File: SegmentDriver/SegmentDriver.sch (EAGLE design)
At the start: 220 parts, among them IC1 PCA9555PW, IC2 ATMEGA644A, IC3 4511D, K1 691313710002, K17 61200621621, K18 61201021621, K2 691322310002, K4 691313710002, K5 691322310002, Q1 MOSFET-NCHANNEL-FDMS5672, Q10 DMP2215L-7, Q11 DMP2215L-7, Q2 MOSFET-NCHANNEL-FDMS5672, Q3 MOSFET-NCHANNEL-FDMS5672, Q4 MOSFET-NCHANNEL-FDMS5672, Q5 MOSFET-NCHANNEL-FDMS5672, Q6 MOSFET-NCHANNEL-FDMS5672, Q7 MOSFET-NCHANNEL-FDMS5672, Q8 MOSFET-NCHANNEL-FDMS5672, Q9 MOSFET-NCHANNEL-FDMS5672, U1 FOD8321, U10 FOD8321, U13 DS1307SO8-TIGHT, U2 FOD8321, U3 FOD8321, U5 FOD8321, U6 FOD8321, U7 FOD8321, U8 FOD8321, U9 FOD8321, X1 32.768kHz

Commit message: routing rtd inputs
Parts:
- removed H9: MOUNT-PAD-ROUND2,0, simbits:MOUNT-PAD-ROUND2,0
- removed KB1: 53261-03, con-molex:53261-03
- removed KT1, KT2: 691210910004, Wurth_Elektronik_Electromechanic_Terminal_Blocks_Connectors_rev15d:691210910004
- removed LED8: AMBER, adafruit:LEDCHIPLED_0603
- removed Q10: DMP2215L-7, simbits:DMP2215L-7
- removed R69: 33R, simbits:EXBV8V330JV
- added $2_206_$_2016-11-07_20-18-07: MOUNT-HOLE2.0, simbits:MOUNT-HOLE2.0
- added K6: 61200621621, Wire-to-Board:61200621621
- added K7: 61201021621, Wire-to-Board:61201021621
- added LED4: (no value), adafruit:LEDCHIPLED_0603
- added R61: 1k, simbits:EXBV8V330JV
- added U17: (no value), LINE_DRIVERS:ISL83078E
- added Y2: 32.768kHz, SparkFun-FreqCtrl:CRYSTALEPSONMC146
- C1: value 0.1uF -> 470UF; device rcl:C-EUC1206K -> Panasonic-EEEFK_EEEFP:EEE-FK1J471AM-CASE-J16; OC_FARNELL (none) -> 2284670
- C11: value 220UF -> 12pF; device Panasonic-EEEFK_EEEFP:EEE-FK1J221AQ-CASE-H13 -> rcl:C-EUC0603K
- C12: value 0.1uF -> 12pF; device rcl:C-EUC1206K -> rcl:C-EUC0603K
- C13, C6: value 220UF -> 0.1uF; device Panasonic-EEEFK_EEEFP:EEE-FK1J221AQ-CASE-H13 -> rcl:C-EUC0603K
- C14, C5, C7, C8, C9: device rcl:C-EUC1206K -> rcl:C-EUC0603K
- C15, C17, C18: value 220UF -> 0.1uF; device Panasonic-EEEFK_EEEFP:EEE-FK1J221AQ-CASE-H13 -> rcl:C-EUC1206K
- C19, C20, C21, C22, C23: device rcl:C-EUC0603K -> rcl:C-EUC1206K
- C2: value 0.1uF -> 220UF; device rcl:C-EUC1206K -> Panasonic-EEEFK_EEEFP:EEE-FP1V221AP-CASE-F
- C24, C26, C27, C28, C29, C30: value 0.1uF -> 220UF; device rcl:C-EUC0603K -> Panasonic-EEEFK_EEEFP:EEE-FK1J221AQ-CASE-H13
- C3: value 220UF -> 470UF; device Panasonic-EEEFK_EEEFP:EEE-FK1J221AQ-CASE-H13 -> Panasonic-EEEFK_EEEFP:EEE-FK1J471AM-CASE-J16
- C31, C32: value 12pF -> 220UF; device rcl:C-EUC0603K -> Panasonic-EEEFK_EEEFP:EEE-FK1J221AQ-CASE-H13
- C34, C37, C60: value 1uF -> 0.1uF
- C39, C40, C41: value 0.1uF -> 1uF
- C4: device Panasonic-EEEFK_EEEFP:EEE-FK1J221AQ-CASE-H13 -> Panasonic-EEEFK_EEEFP:EEE-FP1V221AP-CASE-F
- C72, C76: value 470UF -> 0.1uF; device Panasonic-EEEFK_EEEFP:EEE-FK1J471AM-CASE-J16 -> rcl:C-EUC0603K
- C74, C75: value 220UF -> 0.1uF; device Panasonic-EEEFK_EEEFP:EEE-FP1V221AP-CASE-F -> rcl:C-EUC0603K
- H5: value MOUNT-HOLE2.0 -> MOUNT-PAD-ROUND2,0; device simbits:MOUNT-HOLE2.0 -> simbits:MOUNT-PAD-ROUND2,0
- IC1: value PCA9555PW -> ATMEGA644A; device micro-philips:PCA9555PW -> atmel:ATMEGA644A
- IC2: value ATMEGA644A -> PCA9555PW; device atmel:ATMEGA644A -> micro-philips:PCA9555PW
- K17: value 61200621621 -> 691210910004; device Wire-to-Board:61200621621 -> Wurth_Elektronik_Electromechanic_Terminal_Blocks_Connectors_rev15d:691210910004
- K18: value 61201021621 -> 691210910004; device Wire-to-Board:61201021621 -> Wurth_Elektronik_Electromechanic_Terminal_Blocks_Connectors_rev15d:691210910004
- K2: value 691322310002 -> 691313710002; device Wurth_Elektronik_Electromechanic_Terminal_Blocks_Connectors_rev15d:691322310002 -> Wurth_Elektronik_Electromechanic_Terminal_Blocks_Connectors_rev15d:691313710002
- K3: value (none) -> 691322310002; device Wurth_Elektronik_Electromechanic_Input-Output_Connectors_rev15c:615016149521 -> Wurth_Elektronik_Electromechanic_Terminal_Blocks_Connectors_rev15d:691322310002
- K4: value 691313710002 -> 691322310002; device Wurth_Elektronik_Electromechanic_Terminal_Blocks_Connectors_rev15d:691313710002 -> Wurth_Elektronik_Electromechanic_Terminal_Blocks_Connectors_rev15d:691322310002
- K5: value 691322310002 -> (none); device Wurth_Elektronik_Electromechanic_Terminal_Blocks_Connectors_rev15d:691322310002 -> Wurth_Elektronik_Electromechanic_Input-Output_Connectors_rev15c:615016149521
- LED1: value 7-SEG_SA02-107 -> (none); device display-kingbright-2:7-SEG_SA02-107 -> adafruit:LEDCHIPLED_0603
- LED5, LED6: value (none) -> AMBER
- LED7: value AMBER -> 7-SEG_SA02-107; device adafruit:LEDCHIPLED_0603 -> display-kingbright-2:7-SEG_SA02-107
- R1: value 330 -> 2K4
- R10: value 10k -> 330
- R11, R12: value 100k -> 330
- R13, R14, R15, R16, R17: value 0R -> 330
- R18: value 1k -> 330
- R19, R20, R21, R29, R30, R34, R36: value 0R -> 100k
- R2: value 330 -> 1.2K
- R22, R23, R24, R25, R26, R27: value 0R -> 33R; device rcl:R-EU_R0603 -> simbits:EXBV8V330JV; MPN (none) -> EXBV8V470JV
- R28: value 10k -> 100k
- R3, R9: value 330 -> 10k
- R31, R35: value 1k -> 100k
- R32, R33: value 4.7k -> 100k
- R37, R38, R39, R40, R41, R42, R43, R44, R45, R46: value 100k -> 0R
- R4, R7, R8: value 330 -> 1k
- R47: value 1.2K -> 0R
- R48: value 2K4 -> 0R
- R49, R50, R51, R52: value 33R -> 0R; device simbits:EXBV8V330JV -> rcl:R-EU_R0603; MPN EXBV8V470JV -> (none)
- R5, R6: value 330 -> 4.7k
- R53, R54: value 1k -> 0R
- R55: value 33R -> 1k; device simbits:EXBV8V330JV -> rcl:R-EU_R0603; MPN EXBV8V470JV -> (none)
- R56: value 47R -> 1k; device simbits:EXBV8V330JV -> rcl:R-EU_R0603; MPN EXBV8V470JV -> (none)
- R57: value 47R -> 10k; device simbits:EXBV8V330JV -> rcl:R-EU_R0603; MPN EXBV8V470JV -> (none)
- R58: value 10k -> 47R; device rcl:R-EU_R0603 -> simbits:EXBV8V330JV; MPN (none) -> EXBV8V470JV
- R59: MPN EXBV8V102JV -> EXBV8V470JV
- R60: value 1k -> 47R
- U1: value FOD8321 -> DS1307SO8-TIGHT; device simbits:FOD8321 -> SparkFun-FreqCtrl:DS1307SO8-TIGHT
- U11: value (none) -> FOD8321; device simbits:ADS1X48IPW -> simbits:FOD8321
- U13: value DS1307SO8-TIGHT -> (none); device SparkFun-FreqCtrl:DS1307SO8-TIGHT -> simbits:ADS1X48IPW
- U15: value (none) -> DMP2215L-7; device LINE_DRIVERS:ISL83078E -> simbits:DMP2215L-7
- U2: value FOD8321 -> (none); device simbits:FOD8321 -> adafruit:PCA9685
- U4: value (none) -> FOD8321; device adafruit:PCA9685 -> simbits:FOD8321
- X1: value 32.768kHz -> 53261-03; device SparkFun-FreqCtrl:CRYSTALEPSONMC146 -> con-molex:53261-03
- renumbered KB2 to X2, KB3 to X3, KB4 to X4, KB5 to X5, KB6 to X6, KD1 to K15, KD2 to K16, KS1 to K8, KS2 to K9, KS3 to K10, KS4 to K11, KS5 to K12, KS6 to K13, KS7 to K14, KT3 to K19, KT4 to K20, KT5 to K21, KT6 to K22, KT7 to K23, KTD1 to K24, KTD2 to K25, Q11 to U16, RESET_SW to SW1
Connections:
- removed net N$77: R52.5, U12.SCLK@28
- removed net N$78: R52.6, U12.DOUT/!DRDY!@26
- removed net N$79: R52.7, U12.DIN@27
- removed net N$80: R52.8, U12.!CS!@24
- removed net N$81: R55.5, U12.!DRDY!@25
- removed net N$82: R55.8, U12.START@23
- new net AD1_REFN0: C43.2, C44.1, R29.2, U12.REFN0/GPIO1@6
- new net AD1_REFP0: C42.2, C43.1, R28.2, U12.REFP0/GPIO0@5
- new net AD2_REFN0: C46.2, C47.1, R31.2, U13.REFN0/GPIO1@6
- new net AD2_REFP0: C45.2, C46.1, R30.2, U13.REFP0/GPIO0@5
- new net AD3_REFN0: C49.2, C50.1, R33.2, U14.REFN0/GPIO1@6
- new net AD3_REFP0: C48.2, C49.1, R32.2, U14.REFP0/GPIO0@5
- net !RESET: now also IC1.RESET, K6.5, K7.6, R3.1; no longer IC2.RESET, K17.5, K18.6, R28.1
- net +12V: now also C15.1, C17.1, C18.1, C19.1, C20.1, C21.1, C22.1, C23.1, C4.1, C6.2, K3.1, K4.2, R2.2, U11.VDD@6, U4.VDD@6; no longer C1.1, C12.1, C14.1, C5.1, C7.1, C74.1, C75.1, C77.2, C8.1, C9.1, K2.1, K5.2, R47.2, U1.VDD@6, U2.VDD@6
- net +24V: now also C1.1, C3.1, C5.2, K2.2, R1.2; no longer C72.1, C76.1, C78.2, K4.2, R48.2
- net +5V: now also C14.1, C78.1, IC2.VDD, R57.2, R9.2, U15.S, U17.VCC, U2.VDD, X1-1.S; no longer C10.1, C73.1, IC1.VDD, KB1-1.S, Q10.S, R10.2, R58.2, U15.VCC, U4.VDD
- net 5V: now also C10.2, C7.2, C8.2, C9.2, IC1.AVCC, IC1.VCC, IC1.VCC@1, IC1.VCC@2, K6.2, K7.4, R3.2, R5.2, R6.2, U1.VCC; no longer C26.2, C27.2, C28.2, C30.2, IC2.AVCC, IC2.VCC, IC2.VCC@1, IC2.VCC@2, K17.2, K18.4, R28.2, R32.2, R33.2, U13.VCC
- net AD1_!CS: now also R22.2; no longer R69.1
- net AD1_!DRDY: now also R22.3; no longer R49.4
- net AD1_!RESET: now also R19.1, U12.!RESET!@4; no longer R11.1, U11.!RESET!@4
- net AD1_AIN0: now also K17.4, U12.AIN0/IEXC@11; no longer KT1.4, U11.AIN0/IEXC@11
- net AD1_AIN1: now also C51.2, C54.1, R37.1, U12.AIN1/IEXC@12; no longer C19.2, C20.1, R13.1, U11.AIN1/IEXC@12
- net AD1_AIN2: now also C51.1, C57.2, R38.1, U12.AIN2/IEXC/GPIO2@17; no longer C19.1, C22.2, R14.1, U11.AIN2/IEXC/GPIO2@17
- net AD1_AIN3: now also K18.4, U12.AIN3/IEXC/GPIO3@18; no longer KT2.4, U11.AIN3/IEXC/GPIO3@18
- net AD1_AIN4: now also C52.2, C55.1, R39.1, U12.AIN4/IEXC/GPIO4@13; no longer C23.2, C24.1, R15.1, U11.AIN4/IEXC/GPIO4@13
- net AD1_AIN5: now also C52.1, C58.2, R40.1, U12.AIN5/IEXC/GPIO5@14; no longer C23.1, C38.2, R16.1, U11.AIN5/IEXC/GPIO5@14
- net AD1_AIN6: now also C53.2, C56.1, R41.1, U12.AIN6/IEXC/GPIO6@15; no longer C39.2, C40.1, R17.1, U11.AIN6/IEXC/GPIO6@15
- net AD1_AIN7: now also C53.1, C59.2, R42.1, U12.AIN7/IEXC/GPIO7@16; no longer C39.1, C41.2, R19.1, U11.AIN7/IEXC/GPIO7@16
- net AD1_BIASP: now also K17.1, K18.1, R28.1, R34.2; no longer KT1.1, KT2.1, R38.2, R39.1
- net AD1_IEXC1: now also U12.IEXC1@20
- net AD1_START: now also R22.1; no longer R49.1
- net AD2_!CS: now also R24.2; no longer R52.1
- net AD2_!DRDY: now also R24.3; no longer R55.4
- net AD2_!RESET: now also R20.1, U13.!RESET!@4; no longer R12.1, U12.!RESET!@4
- net AD2_AIN0: now also U13.AIN0/IEXC@11; no longer U12.AIN0/IEXC@11
- net AD2_AIN1: now also C60.2, C63.1, R43.1, U13.AIN1/IEXC@12; no longer C42.2, C43.1, R20.1, U12.AIN1/IEXC@12
- net AD2_AIN2: now also C60.1, C66.2, R44.1, U13.AIN2/IEXC/GPIO2@17; no longer C42.1, C44.2, R21.1, U12.AIN2/IEXC/GPIO2@17
- net AD2_AIN3: now also U13.AIN3/IEXC/GPIO3@18; no longer U12.AIN3/IEXC/GPIO3@18
- net AD2_AIN4: now also C61.2, C64.1, R45.1, U13.AIN4/IEXC/GPIO4@13; no longer C45.2, C46.1, R22.1, U12.AIN4/IEXC/GPIO4@13
- net AD2_AIN5: now also C61.1, C67.2, R46.1, U13.AIN5/IEXC/GPIO5@14; no longer C45.1, C47.2, R23.1, U12.AIN5/IEXC/GPIO5@14
- net AD2_AIN6: now also C62.2, C65.1, R47.1, U13.AIN6/IEXC/GPIO6@15; no longer C48.2, C49.1, R24.1, U12.AIN6/IEXC/GPIO6@15
- net AD2_AIN7: now also C62.1, C68.2, R48.1, U13.AIN7/IEXC/GPIO7@16; no longer C48.1, C50.2, R25.1, U12.AIN7/IEXC/GPIO7@16
- net AD2_BIASP: now also R30.1, R32.1, R35.2, R36.2; no longer R41.2, R42.1, R44.2, R45.1
- net AD2_IEXC1: now also U13.IEXC1@20
- net AD2_START: now also R24.1; no longer R55.1
- net AD3_!CS: now also R26.2; no longer R51.1
- net AD3_!DRDY: now also R26.3; no longer R50.4
- net AD3_!RESET: now also R21.1; no longer R37.1
- net AD3_AIN1: now also C69.2, C72.1, R49.1; no longer C51.2, C52.1, R26.1
- net AD3_AIN2: now also C69.1, C75.2, R50.1; no longer C51.1, C53.2, R27.1
- net AD3_AIN4: now also C70.2, C73.1, R51.1; no longer C54.2, C55.1, R29.1
- net AD3_AIN5: now also C70.1, C76.2, R52.1; no longer C54.1, C56.2, R30.1
- net AD3_AIN6: now also C71.2, C74.1, R53.1; no longer C57.2, C58.1, R34.1
- net AD3_AIN7: now also C71.1, C77.2, R54.1; no longer C57.1, C59.2, R36.1
- net AD3_IEXC1: now also U14.IEXC1@20
- net AD3_START: now also R26.1; no longer R50.1
- net AGND: now also C24.2, C26.2, C27.2, C28.2, C29.2, C30.2, C31.2, C32.2; no longer C11.2, C13.2, C15.2, C17.2, C18.2, C3.2, C4.2, C6.2
- net AVDD: now also C37.1, C38.1, U13.AVDD@22; no longer C33.1, C62.1, U11.AVDD@22
- net CS_ADS1248_1: now also IC1.(PCINT2/ADC2)PA2; no longer IC2.(PCINT2/ADC2)PA2
- net CS_ADS1248_2: now also IC1.(PCINT1/ADC1)PA1; no longer IC2.(PCINT1/ADC1)PA1
- net CS_ADS1248_3: now also IC1.(PCINT0/ADC0)PA0; no longer IC2.(PCINT0/ADC0)PA0
- net DVDD: now also C33.1, C34.1, R19.2, R20.2, R21.2, U13.DVDD@1; no longer C21.1, C61.1, R11.2, R12.2, R37.2, U11.DVDD@1
- net EXTGPIO_!INT: now also IC1.(PCINT27/INT1)PD3, IC2.!INT, R57.1; no longer IC1.!INT, IC2.(PCINT27/INT1)PD3, R58.1
- net GND: now also C10.1, C11.2, C13.1, C15.2, C17.2, C18.2, C19.2, C22.2, C23.2, C3.2, C38.2, C39.2, C4.2, C41.2, C42.1, C44.2, C45.1, C47.2, C48.1, C5.1, C50.2, C54.2, C56.2, C57.1, C58.1, C6.1, C63.2, C64.2, C67.1, C68.1, C7.1, C75.1, C76.1, C78.2, C8.1, C9.1, H5.MOUNT, IC1.GND, IC1.GND@1, IC1.GND@2, IC1.GND@3, IC2.A0, IC2.A1, IC2.A2, IC2.VSS, K2.1, K3.2, K6.6, K7.10, K7.2, LED1.C, LED4.C, LED7.COM@1, LED7.COM@2, R29.1, R31.1, R33.1, R34.1, R35.1, R36.1, R55.1, R56.1, U1.GND, U11.K@3, U11.VSS@4, U13.AVSS@21, U13.CLK@3, U13.DGND@2, U13.VREFCOM@10, U17.GND, U2.A0, U2.A1, U2.A2, U2.A3, U2.A4, U2.A5, U2.EXTCLK, U2.GND, U4.K@3, U4.VSS@4, X1-3.S; no longer C10.2, C22.1, C24.2, C26.1, C27.1, C28.1, C29.1, C30.1, C31.2, C32.2, C38.1, C41.1, C43.2, C44.1, C46.2, C47.1, C49.2, C5.2, C50.1, C52.2, C53.1, C56.1, C58.2, C60.2, C61.2, C62.2, C63.1, C68.2, C69.1, C7.2, C71.2, C75.2, C76.2, C78.1, C8.2, C9.2, H9.MOUNT, IC1.A0, IC1.A1, IC1.A2, IC1.VSS, IC2.GND, IC2.GND@1, IC2.GND@2, IC2.GND@3, K17.6, K18.10, K18.2, K2.2, K5.1, KB1-3.S, LED1.COM@1, LED1.COM@2, LED5.C, LED6.C, R38.1, R40.1, R41.1, R43.1, R44.1, R46.1, R53.1, R54.1, U1.K@3, U1.VSS@4, U11.AVSS@21, U11.CLK@3, U11.DGND@2, U11.VREFCOM@10, U13.GND, U15.GND, U2.K@3, U2.VSS@4, U4.A0, U4.A1, U4.A2, U4.A3, U4.A4, U4.A5, U4.EXTCLK, U4.GND
- net GPIO1: now also R58.8, X1-2.S; no longer KB1-2.S, R56.8
- net GPIO2: now also R58.7; no longer R56.7
- net GPIO3: now also R58.6; no longer R56.6
- net GPIO4: now also R58.5; no longer R56.5
- net GPIO5: now also R59.8; no longer R57.8
- net GPIO6: now also R59.7; no longer R57.7
- net GPIO7: now also R59.6; no longer R57.6
- net GPIO8: now also R59.5; no longer R57.5
- net IIC1_SCL: now also IC1.(PCINT16/SCL)PC0, IC2.SCL, R5.1, U1.SCL, U2.SCL; no longer IC1.SCL, IC2.(PCINT16/SCL)PC0, R32.1, U13.SCL, U4.SCL
- net IIC1_SDA: now also IC1.(PCINT17/SDA)PC1, IC2.SDA, R6.1, U1.SDA, U2.SDA; no longer IC1.SDA, IC2.(PCINT17/SDA)PC1, R33.1, U13.SDA, U4.SDA
- net LED1: now also IC1.(PCINT7/ADC7)PA7, R7.1; no longer IC2.(PCINT7/ADC7)PA7, R35.1
- net LED2: now also IC1.(PCINT6/ADC6)PA6, R8.1; no longer IC2.(PCINT6/ADC6)PA6, R31.1
- net MISO: now also IC1.(PCINT14/MISO)PB6, K6.1, R22.4, R24.4, R26.4; no longer IC2.(PCINT14/MISO)PB6, K17.1, R51.3, R52.3, R69.3
- net MOSI: now also IC1.(PCINT13/MOSI)PB5, K6.4, R23.1, R25.1, R27.1; no longer IC2.(PCINT13/MOSI)PB5, K17.4, R51.2, R52.2, R69.2
- net N$1: now also R18.2, U11.A@1; no longer R8.2, U9.A@1
- net N$10: now also R10.2, U3.A@1; no longer R1.2, U1.A@1
- net N$100: now also LED7.E, R61.8; no longer LED1.E, R60.8
- net N$101: now also LED7.F, R61.7; no longer LED1.F, R60.7
- net N$102: now also LED7.G, R61.6; no longer LED1.G, R60.6
- net N$103: now also LED7.DP, R61.5; no longer LED1.DP, R60.5
- net N$104: now also IC2.I/O1.1; no longer IC1.I/O1.1
- net N$105: now also IC2.I/O1.2; no longer IC1.I/O1.2
- net N$106: now also IC2.I/O1.3; no longer IC1.I/O1.3
- net N$107: now also IC2.I/O1.4; no longer IC1.I/O1.4
- net N$108: now also IC2.I/O1.5, R61.4; no longer IC1.I/O1.5, R60.4
- net N$11: now also C27.1; no longer C11.1
- net N$12: now also R14.2, U7.A@1; no longer R5.2, U6.A@1
- net N$13: now also C28.1; no longer C13.1
- net N$14: now also R15.2, U8.A@1; no longer R6.2, U7.A@1
- net N$15: now also C29.1; no longer C15.1
- net N$16: now also R16.2, U9.A@1; no longer R7.2, U8.A@1
- net N$17: now also C30.1; no longer C17.1
- net N$18: now also C31.1, Q8.D; no longer C18.1, Q9.D
- net N$19: now also C32.1, Q9.D; no longer C25.1, Q8.D
- net N$2: now also R17.2; no longer R9.2
- net N$20: now also K18.3, R39.2; no longer KT2.3, R15.2
- net N$21: now also U1.X2, Y2.1; no longer U13.X2, X1.1
- net N$22: now also K18.2, R40.2; no longer KT2.2, R16.2
- net N$23: now also K17.3, R37.2; no longer KT1.3, R13.2
- net N$24: now also U1.VBATT; no longer U13.VBATT
- net N$25: now also LED5.C, R55.2; no longer LED7.C, R53.2
- net N$26: now also LED6.C, R56.2; no longer LED8.C, R54.2
- net N$27: now also K17.2, R38.2; no longer KT1.2, R14.2
- net N$28: now also R41.2; no longer R17.2
- net N$29: now also C13.2, IC1.AREF; no longer C29.2, IC2.AREF
- net N$3: now also C24.1; no longer C3.1
- net N$30: now also C39.1, U12.VREFOUT@9; no longer C34.1, U11.VREFOUT@9
- net N$31: now also R42.2; no longer R19.2
- net N$32: now also LED4.A, R8.2; no longer LED5.A, R31.2
- net N$33: now also LED3.A, R7.2; no longer LED6.A, R35.2
- net N$34: now also R43.2; no longer R20.2
- net N$35: now also R44.2; no longer R21.2
- net N$36: now also IC2.I/O0.0, R58.1; no longer IC1.I/O0.0, R56.1
- net N$37: now also IC2.I/O0.1, R58.2; no longer IC1.I/O0.1, R56.2
- net N$38: now also IC2.I/O0.2, R58.3; no longer IC1.I/O0.2, R56.3
- net N$39: now also C12.1, IC1.XTAL1; no longer C32.1, IC2.XTAL1
- net N$4: now also R11.2, U4.A@1; no longer R2.2, U2.A@1
- net N$40: now also C11.1, IC1.XTAL2; no longer C31.1, IC2.XTAL2
- net N$41: now also C40.1, U13.VREFOUT@9; no longer C37.1, U12.VREFOUT@9
- net N$42: now also R45.2; no longer R22.2
- net N$43: now also R46.2; no longer R23.2
- net N$44: now also R47.2; no longer R24.2
- net N$45: now also R48.2; no longer R25.2
- net N$46: now also R49.2; no longer R26.2
- net N$47: now also IC1.(PCINT24/RXD0)PD0, R4.2; no longer IC2.(PCINT24/RXD0)PD0, R18.2
- net N$48: now also R50.2; no longer R27.2
- net N$49: now also R51.2; no longer R29.2
- net N$5: now also R9.1, U2.#OE; no longer R10.1, U4.#OE
- net N$50: now also R52.2; no longer R30.2
- net N$51: now also R53.2; no longer R34.2
- net N$52: now also R54.2; no longer R36.2
- net N$53: now also C41.1; no longer C60.1
- net N$54: now also R23.7, U12.SCLK@28; no longer C67.2, C68.1, R43.2, U12.REFN0/GPIO1@6
- net N$55: now also R23.8, U12.DIN@27; no longer C64.2, C65.1, R40.2, U11.REFN0/GPIO1@6
- net N$56: now also R22.5, U12.DOUT/!DRDY!@26; no longer C66.2, C67.1, R42.2, U12.REFP0/GPIO0@5
- net N$57: now also R22.6, U12.!DRDY!@25; no longer C63.2, C64.1, R39.2, U11.REFP0/GPIO0@5
- net N$58: now also R22.7, U12.!CS!@24; no longer C70.2, C71.1, R46.2, U14.REFN0/GPIO1@6
- net N$59: now also R22.8, U12.START@23; no longer C69.2, C70.1, R45.2, U14.REFP0/GPIO0@5
- net N$6: now also C25.1; no longer C4.1
- net N$60: now also LED5.A, U15.D; no longer LED7.A, Q10.D
- net N$61: now also LED6.A; no longer LED8.A
- net N$62: now also LED2.A, R2.1; no longer LED3.A, R47.1
- net N$63: now also LED1.A, R1.1; no longer LED2.A, R48.1
- net N$64: now also U17.RE; no longer U15.RE
- net N$65: now also R24.8, U13.START@23; no longer R49.5, U11.!DRDY!@25
- net N$66: now also R24.6, U13.!DRDY!@25; no longer R69.8, U11.!CS!@24
- net N$67: now also R24.7, U13.!CS!@24; no longer R69.7, U11.DIN@27
- net N$68: now also R25.8, U13.DIN@27; no longer R69.6, U11.DOUT/!DRDY!@26
- net N$69: now also R24.5, U13.DOUT/!DRDY!@26; no longer R69.5, U11.SCLK@28
- net N$7: now also R12.2, U5.A@1; no longer R3.2, U3.A@1
- net N$70: now also R25.7, U13.SCLK@28; no longer R49.8, U11.START@23
- net N$71: now also R26.8, U14.START@23; no longer R51.5, U14.SCLK@28
- net N$72: now also R26.6, U14.!DRDY!@25; no longer R51.6, U14.DOUT/!DRDY!@26
- net N$73: now also R26.7, U14.!CS!@24; no longer R51.7, U14.DIN@27
- net N$74: now also R27.8, U14.DIN@27; no longer R51.8, U14.!CS!@24
- net N$75: now also R26.5, U14.DOUT/!DRDY!@26; no longer R50.5, U14.!DRDY!@25
- net N$76: now also R27.7, U14.SCLK@28; no longer R50.8, U14.START@23
- net N$8: now also C26.1; no longer C6.1
- net N$83: now also IC2.I/O0.3, R58.4; no longer IC1.I/O0.3, R56.4
- net N$84: now also IC2.I/O0.4, R59.1; no longer IC1.I/O0.4, R57.1
- net N$85: now also IC2.I/O0.5, R59.2; no longer IC1.I/O0.5, R57.2
- net N$86: now also IC2.I/O0.6, R59.3; no longer IC1.I/O0.6, R57.3
- net N$87: now also IC2.I/O0.7, R59.4; no longer IC1.I/O0.7, R57.4
- net N$88: now also IC2.I/O1.0; no longer IC1.I/O1.0
- net N$89: now also R60.1; no longer R59.1
- net N$9: now also R13.2, U6.A@1; no longer R4.2, U5.A@1
- net N$90: now also R60.2; no longer R59.2
- net N$91: now also R60.3; no longer R59.3
- net N$92: now also R60.4; no longer R59.4
- net N$93: now also R61.1; no longer R60.1
- net N$94: now also R61.2; no longer R60.2
- net N$95: now also R61.3; no longer R60.3
- net N$96: now also LED7.A, R60.8; no longer LED1.A, R59.8
- net N$97: now also LED7.B, R60.7; no longer LED1.B, R59.7
- net N$98: now also LED7.C, R60.6; no longer LED1.C, R59.6
- net N$99: now also LED7.D, R60.5; no longer LED1.D, R59.5
- net PWM_DOT1: now also R17.1, U2.PWM7; no longer R9.1, U4.PWM7
- net PWM_DOT2: now also R18.1, U2.PWM8; no longer R8.1, U4.PWM8
- net PWM_SEG1: now also R10.1, U2.PWM0; no longer R1.1, U4.PWM0
- net PWM_SEG2: now also R11.1, U2.PWM1; no longer R2.1, U4.PWM1
- net PWM_SEG3: now also R12.1, U2.PWM2; no longer R3.1, U4.PWM2
- net PWM_SEG4: now also R13.1, U2.PWM3; no longer R4.1, U4.PWM3
- net PWM_SEG5: now also R14.1, U2.PWM4; no longer R5.1, U4.PWM4
- net PWM_SEG6: now also R15.1, U2.PWM5; no longer R6.1, U4.PWM5
- net PWM_SEG7: now also R16.1, U2.PWM6; no longer R7.1, U4.PWM6
- net RS485+: now also K5.A2, K5.B1, U17.A/Y; no longer K3.A2, K3.B1, U15.A/Y
- net RS485-: now also K5.A1, K5.B2, U17.B/Z; no longer K3.A1, K3.B2, U15.B/Z
- net RTC_1HZ_CLK: now also IC1.(PCINT26/INT0)PD2, U1.SQW; no longer IC2.(PCINT26/INT0)PD2, U13.SQW
- net SCK: now also IC1.(PCINT15/SCK)PB7, K6.3, R23.2, R25.2, R27.2; no longer IC2.(PCINT15/SCK)PB7, K17.3, R51.4, R52.4, R69.4
- net TCK: now also IC1.(PCINT18/TCK)PC2, K7.1; no longer IC2.(PCINT18/TCK)PC2, K18.1
- net TDI: now also IC1.(PCINT21/TDI)PC5, K7.9; no longer IC2.(PCINT21/TDI)PC5, K18.9
- net TDO: now also IC1.(PCINT20/TDO)PC4, K7.3; no longer IC2.(PCINT20/TDO)PC4, K18.3
- net TMS: now also IC1.(PCINT19/TMS)PC3, K7.5; no longer IC2.(PCINT19/TMS)PC3, K18.5
- net UART_DE: now also IC1.(PCINT5/ADC5)PA5, U17.DE; no longer IC2.(PCINT5/ADC5)PA5, U15.DE
- net UART_RX: now also R4.1, U15.G, U17.R0; no longer Q10.G, R18.1, U15.R0
- net UART_TX: now also IC1.(PCINT25/TXD0)PD1, U17.DI; no longer IC2.(PCINT25/TXD0)PD1, U15.DI
- net VO: now also U3.VO@5; no longer U1.VO@5
- net VO1: now also U4.VO@5; no longer U2.VO@5
- net VO2: now also U5.VO@5; no longer U3.VO@5
- net VO3: now also U6.VO@5; no longer U5.VO@5
- net VO4: now also U7.VO@5; no longer U6.VO@5
- net VO5: now also U8.VO@5; no longer U7.VO@5
- net VO6: now also U9.VO@5; no longer U8.VO@5
- net VO7: now also Q9.G, U11.VO@5; no longer Q8.G, U9.VO@5
- net VO8: now also Q8.G; no longer Q9.G
- net X1: now also U1.X1, Y2.2; no longer U13.X1, X1.2

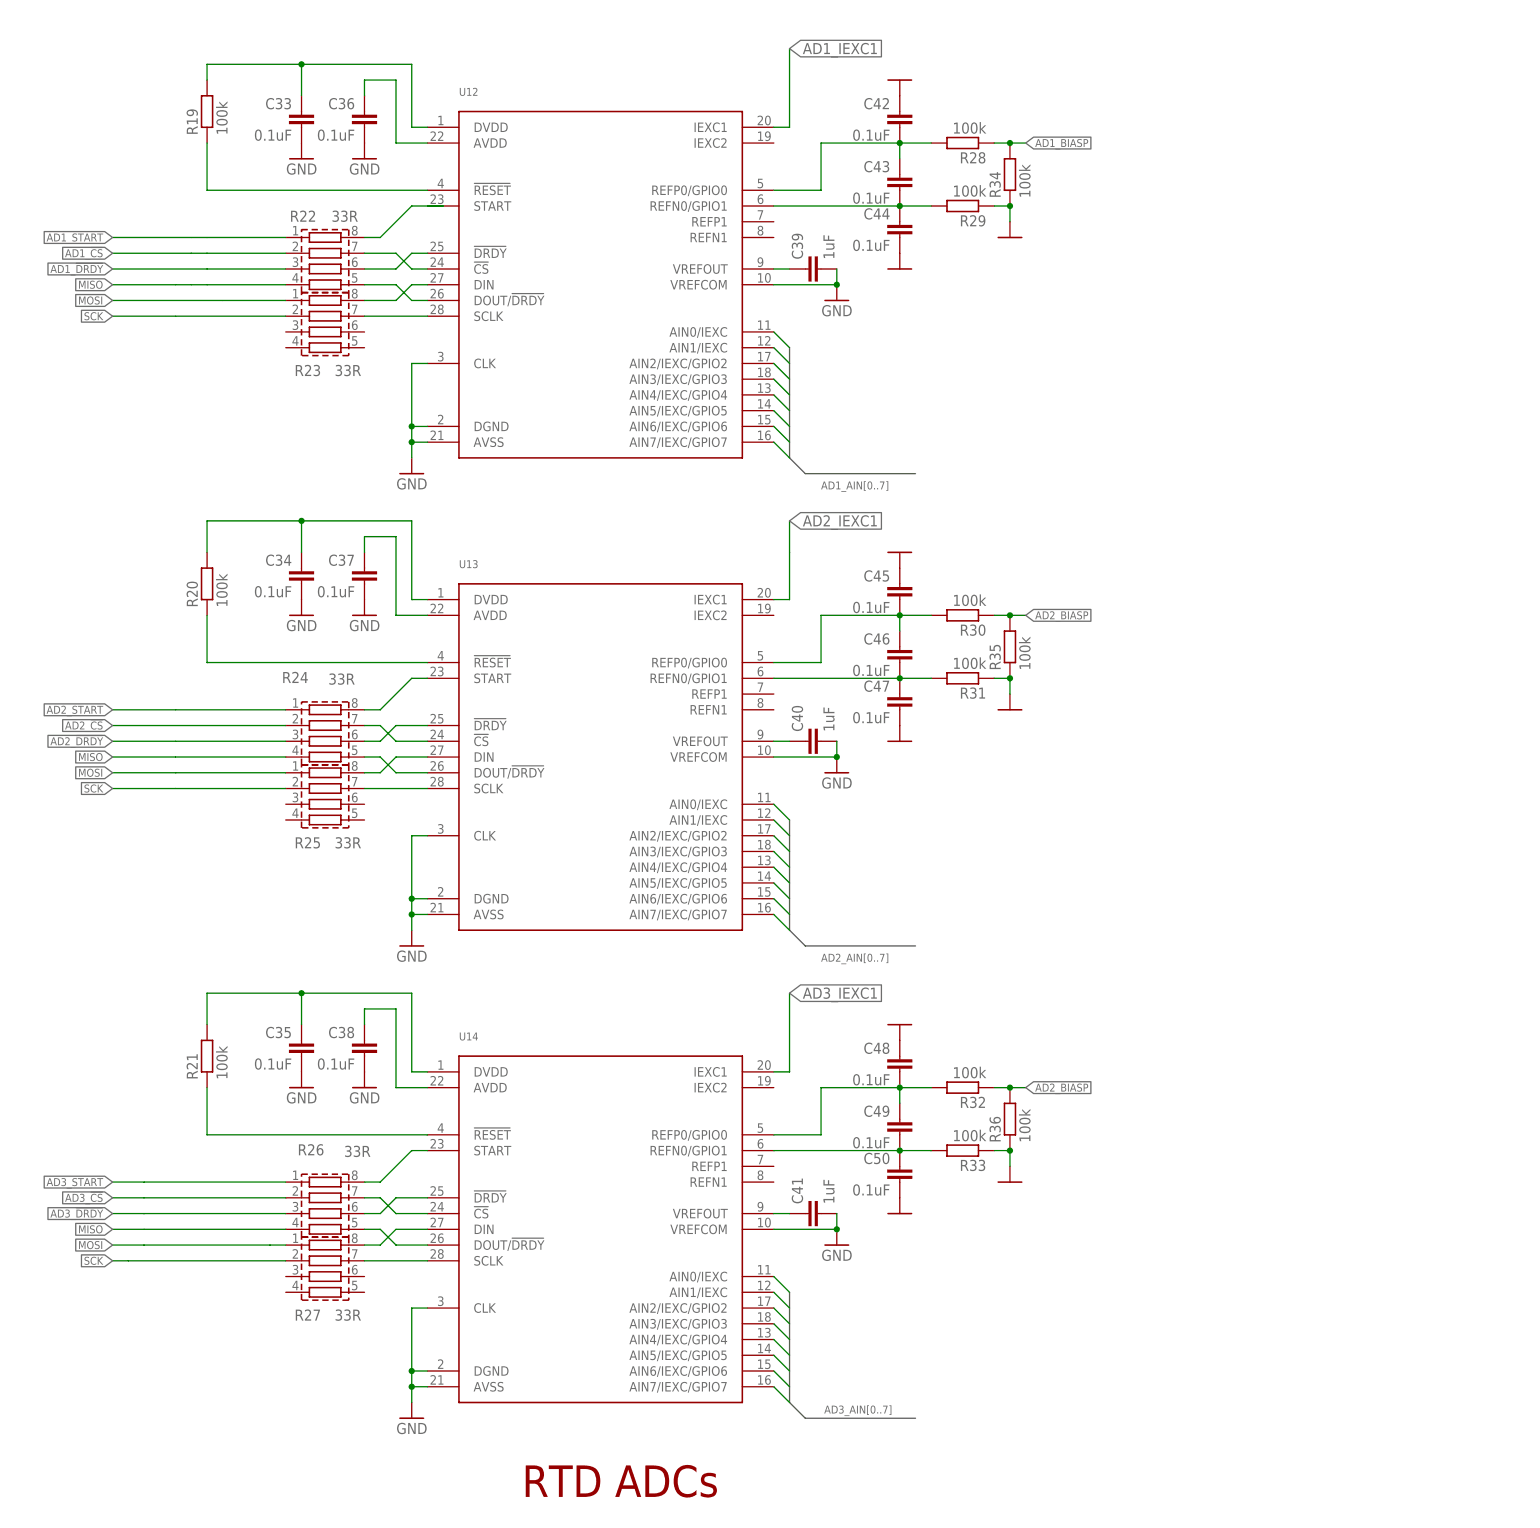
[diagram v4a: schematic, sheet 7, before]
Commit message: RTD AD layout, brd and sch remade consistent
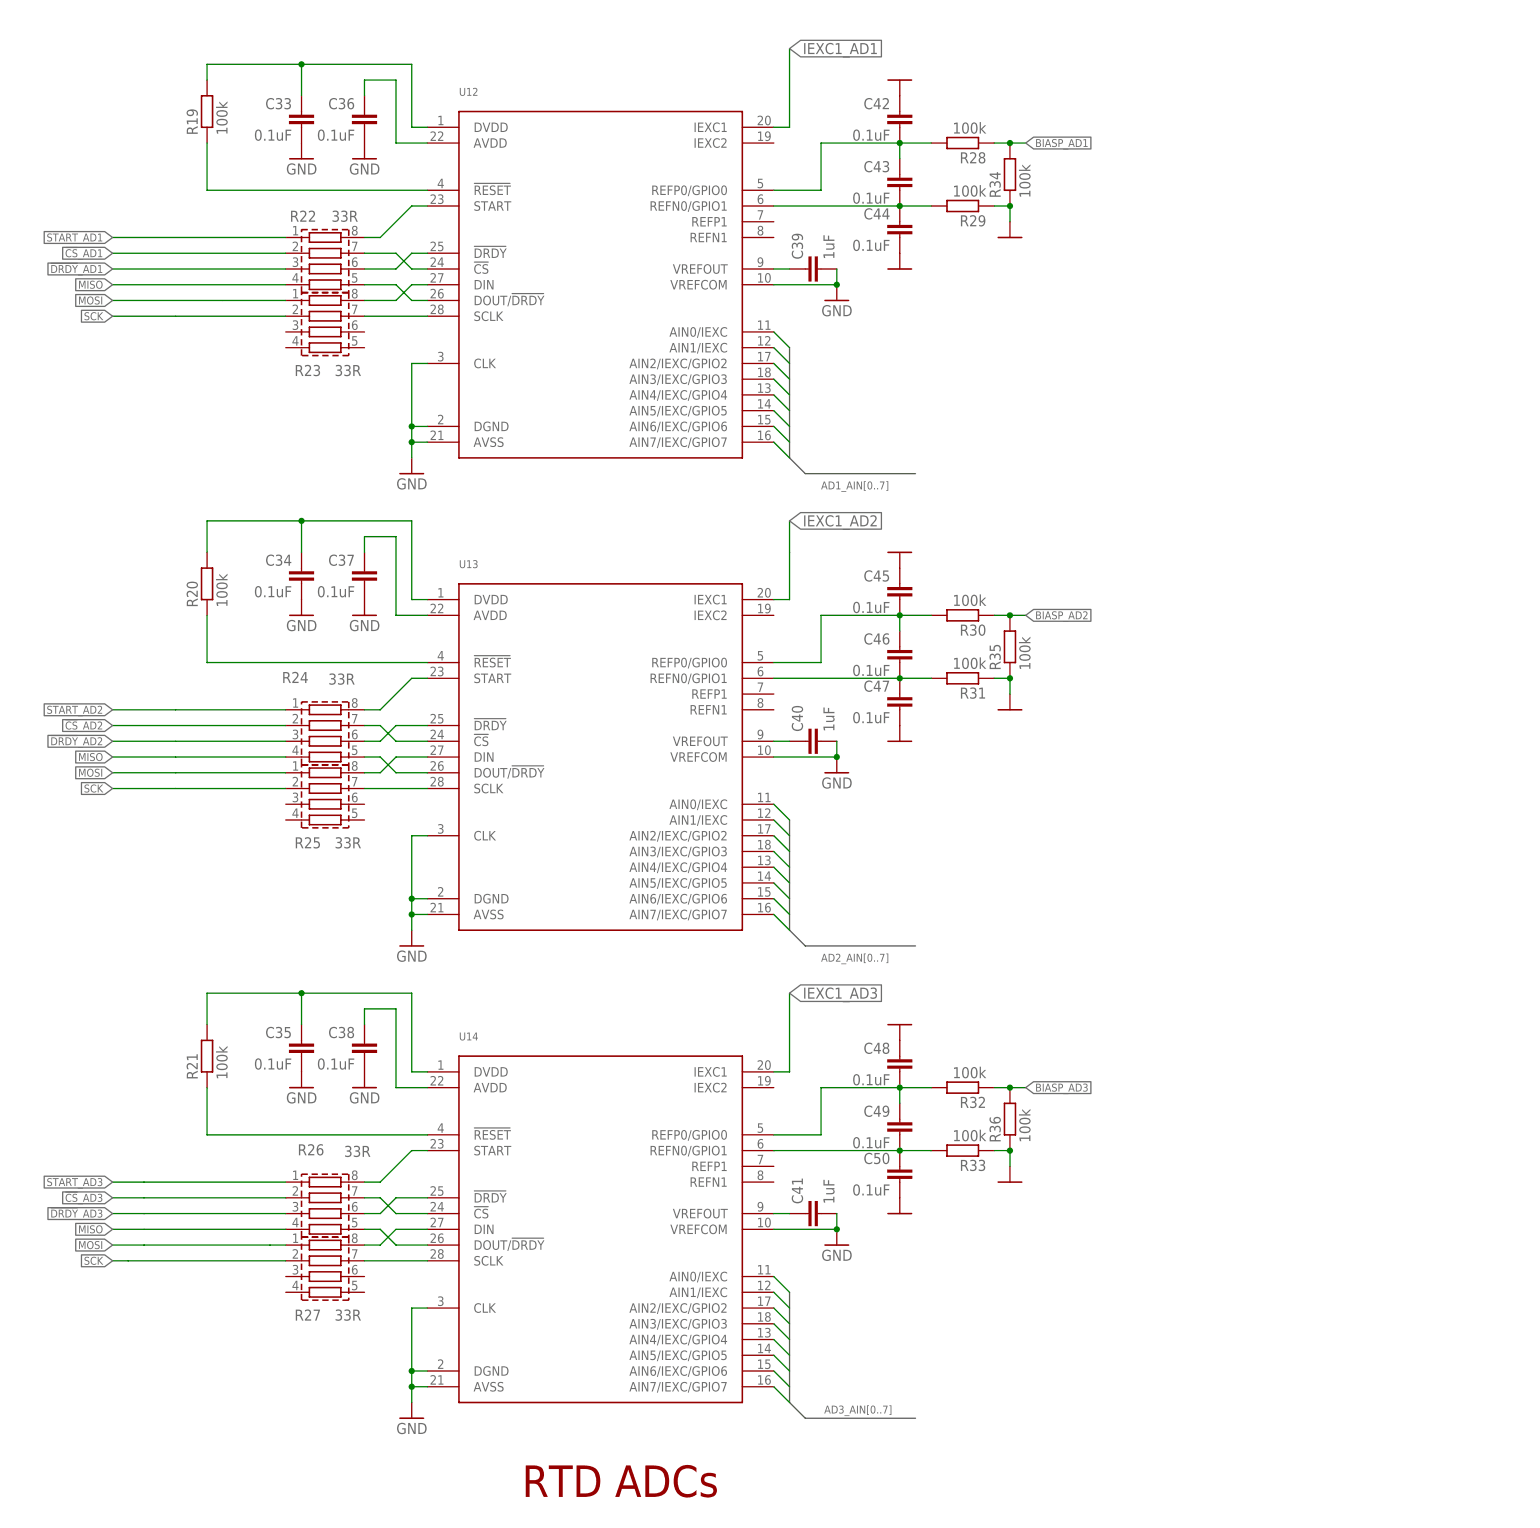
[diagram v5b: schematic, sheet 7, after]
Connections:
- net AD1_!CS renamed !CS!_AD1
- net AD1_!DRDY renamed !DRDY!_AD1
- net AD1_!RESET renamed !RESET!_AD1
- net AD1_BIASP renamed BIASP_AD1
- net AD1_IEXC1 renamed IEXC1_AD1
- net AD1_REFN0 renamed REFN0_AD1
- net AD1_REFP0 renamed REFP0_AD1
- net AD1_START renamed START_AD1
- net AD2_!CS renamed !CS!_AD2
- net AD2_!DRDY renamed !DRDY!_AD2
- net AD2_!RESET renamed !RESET!_AD2
- net AD2_IEXC1 renamed IEXC1_AD2
- net AD2_REFN0 renamed REFN0_AD2
- net AD2_REFP0 renamed REFP0_AD2
- net AD2_START renamed START_AD2
- net AD3_!CS renamed !CS!_AD3
- net AD3_!DRDY renamed !DRDY!_AD3
- net AD3_!RESET renamed !RESET!_AD3
- net AD3_IEXC1 renamed IEXC1_AD3
- net AD3_REFN0 renamed REFN0_AD3
- net AD3_REFP0 renamed REFP0_AD3
- net AD3_START renamed START_AD3
- net N$30 renamed 9_AD1
- net N$41 renamed 9_AD2
- net N$53 renamed 9_AD3
- net N$54 renamed 28_AD1
- net N$55 renamed 27_AD1
- net N$56 renamed 26_AD1
- net N$57 renamed 25_AD1
- net N$58 renamed 24_AD1
- net N$59 renamed 23_AD1
- net N$65 renamed 23_AD2
- net N$66 renamed 25_AD2
- net N$67 renamed 24_AD2
- net N$68 renamed 27_AD2
- net N$69 renamed 26_AD2
- net N$70 renamed 28_AD2
- net N$71 renamed 23_AD3
- net N$72 renamed 25_AD3
- net N$73 renamed 24_AD3
- net N$74 renamed 27_AD3
- net N$75 renamed 26_AD3
- net N$76 renamed 28_AD3
- removed net AD2_BIASP: K20.1, K21.1, K22.1, R30.1, R32.1, R35.2, R36.2
- removed net AD3_BIASP: K23.1, K24.1, K25.1
- new net BIASP_AD2: K20.1, K21.1, K22.1, R30.1, R35.2
- new net BIASP_AD3: K23.1, K24.1, K25.1, R32.1, R36.2
